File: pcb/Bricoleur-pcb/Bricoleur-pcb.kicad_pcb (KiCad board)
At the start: 2 copper layers, 78 parts, among them J1 USB_B_Micro, J2 Conn_02x10_Odd_Even, J3 Conn_02x03_Odd_Even, J4 Conn_02x03_Odd_Even, SW2 SW_Push, SW3 SW_Push, SW4 SW_Push, SW5 SW_Push, U1 Ultrasonic-LV-EZ0, U11 SW_DP3T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

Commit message: USB and some other connections, will probably require polish
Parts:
- moved L1 34.1 mm to (82.1, 119.6)
- moved U9 33.2 mm to (88.6, 117.3)
- moved J1 20.5 mm to (96.4, 115.6)
- moved R5 19.1 mm to (57.1, 170.3)
- moved R6 19.1 mm to (73.4, 170.3)
- moved R7 19.1 mm to (89.9, 170.3)
- moved SW4 19.1 mm to (60.4, 168.8)
- moved SW5 19.1 mm to (76.9, 168.8)
- moved SW2 19.1 mm to (38.9, 173.4)
- moved C14 19.1 mm to (56.9, 166.8)
- moved C16 19.1 mm to (90.4, 166.7)
- moved R1 19.1 mm to (41.6, 172.9)
- moved R11 19.1 mm to (57.1, 172.6)
- moved R12 19.1 mm to (73.4, 172.6)
- moved R13 19.1 mm to (89.9, 172.6)
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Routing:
- net VMCU: track 180.1 -> 294.1 mm, vias 12 -> 13
- net DH_#RESET: track 22.9 -> 91.4 mm, vias 0 -> 2
- net DEBUG_EXT_CABLE_ATTACH: track 0.00 -> 62.8 mm, vias 0 -> 2
- net DH_TCK_SWCLK: track 19.9 -> 77.0 mm, vias 0 -> 3
- net GND: track 210.4 -> 260.0 mm, vias 12 -> 11
- net Net-(C1-Pad2): track 10.2 -> 59.1 mm, vias 0 -> 2
- net /USB_D-: track 0.00 -> 42.3 mm, vias 0 -> 2
- net /USB_D+: track 0.00 -> 40.2 mm
- net DH_TDO_SWO: track 9.26 -> 48.6 mm, vias 0 -> 2
- net DH_TMS_SWDIO: track 9.20 -> 41.8 mm, vias 0 -> 2
- net DBG_PB_3: track 21.7 -> 53.5 mm
- net /sheet5BB7B6EA/INP: track 9.47 -> 38.7 mm
- net Net-(C2-Pad2): track 8.44 -> 37.3 mm, vias 0 -> 2
- net /Sheet5BB71F0E/INP: track 9.34 -> 37.7 mm
- net DBG_PB_1: track 21.1 -> 48.7 mm
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
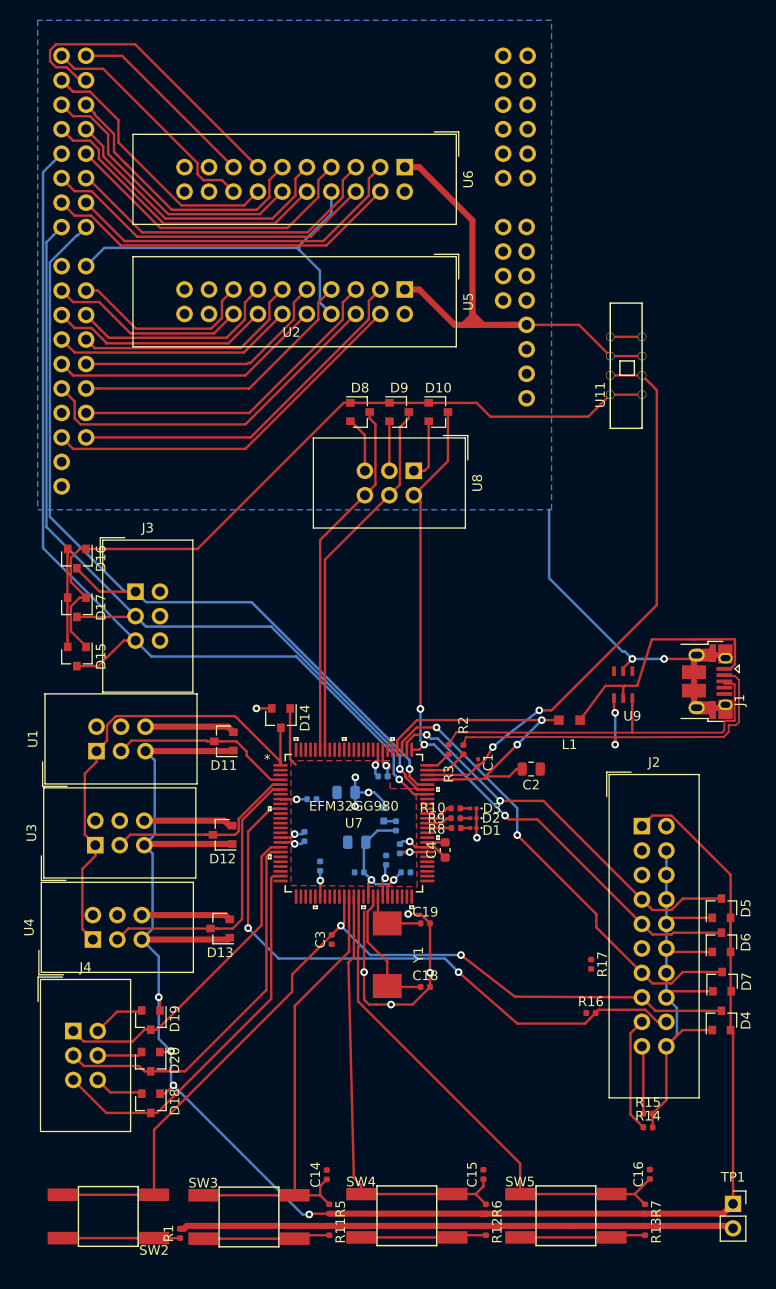
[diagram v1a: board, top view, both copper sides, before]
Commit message: Some routing tweaks
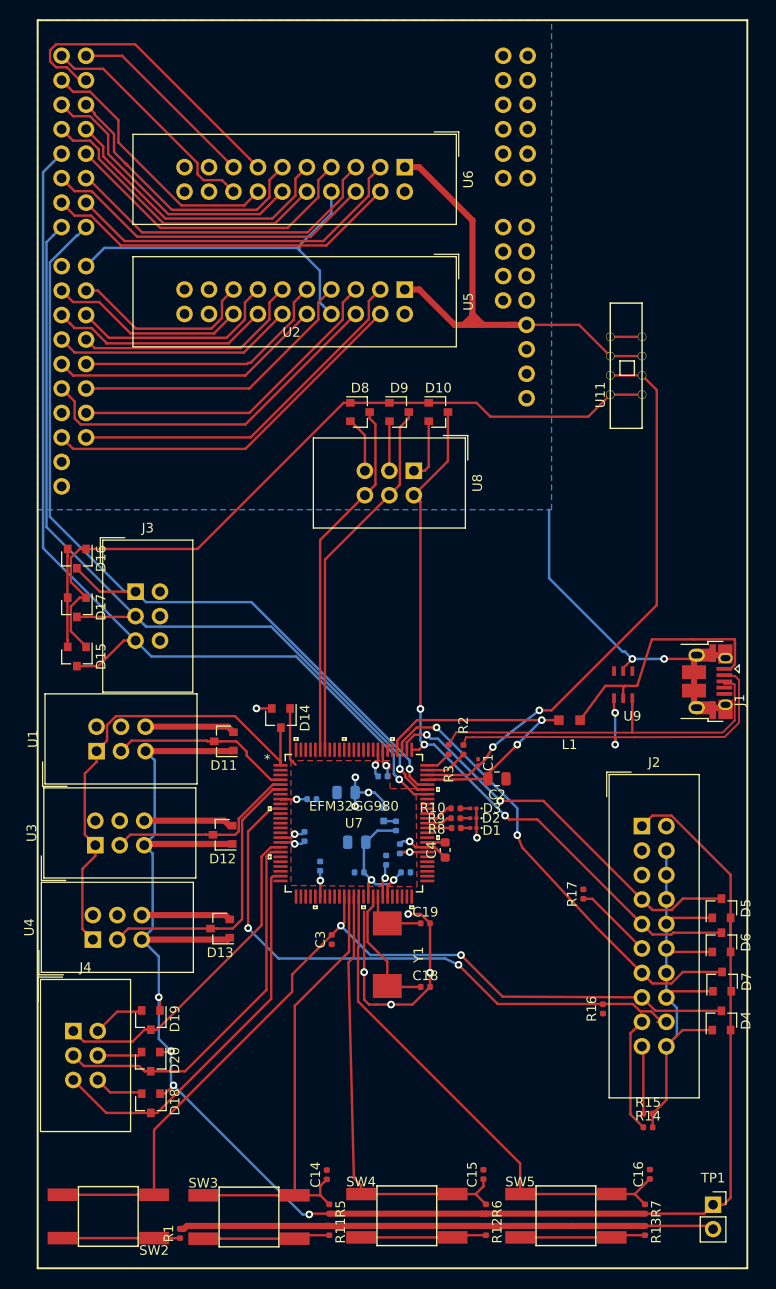
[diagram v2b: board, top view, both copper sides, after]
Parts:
- moved R17 7.33 mm to (83.5, 137.7), turned to 90 degrees
- moved C2 3.70 mm to (74.5, 125.7)
- moved TP1 2.08 mm to (97.0, 169.9)
- moved R16 1.32 mm to (85.5, 149.6), turned to 90 degrees
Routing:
- net Net-(J2-Pad11): track 0.00 -> 8.21 mm
- net Net-(C2-Pad2): track 37.3 -> 33.2 mm
- net GND: track 260.0 -> 258.0 mm
- net /USB_D+: track 40.2 -> 39.5 mm
- net /USB_D-: track 42.3 -> 41.7 mm

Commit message: Overwrite
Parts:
- moved TP1 73.7 mm to (72.6, 100.3), turned to 90 degrees
- moved SW2 35.2 mm to (57.8, 143.6), turned to 270 degrees
- moved R1 27.3 mm to (60.4, 153.1), turned to 0 degrees
- moved U11 23.9 mm to (72.6, 105.4), turned to 0 degrees
- moved D10 18.0 mm to (65.4, 105.4)
- moved D8 18.0 mm to (57.3, 105.4)
- moved D9 18.0 mm to (61.3, 105.4)
- moved U8 18.0 mm to (62.9, 111.5)
- moved J1 14.2 mm to (82.4, 117.9), turned to 90 degrees
- moved R16 10.7 mm to (74.9, 148.7), turned to 0 degrees
- moved U9 10.5 mm to (78.3, 119.6)
- moved C14 9.81 mm to (47.7, 163.2)
- moved C16 9.81 mm to (81.3, 163.2)
- moved R12 9.81 mm to (64.2, 169.0)
- moved R13 9.81 mm to (80.8, 169.0)
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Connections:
- net Net-(J1-Pad1) renamed /USB_5v
- net Net-(R2-Pad1) renamed /USB_R_D+
- net Net-(R3-Pad2) renamed /USB_R_D-
- R16 pad 1: PYNQ_3V3 -> VMCU
- U2 pad 50: /CAM0_DOUT2 -> /CAM0_DOUT3
- U2 pad 57: /CAM0_DOUT5 -> /CAM0_DOUT2
- U2 pad 58: /CAM0_DOUT3 -> /CAM0_DOUT5
- U9 pad 3: (no net) -> /USB_D+
- U9 pad 4: /USB_D+ -> (no net)
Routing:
- net VMCU: track 293.7 -> 342.9 mm, vias 13 -> 15
- net Net-(C1-Pad2): track 59.1 -> 26.2 mm, vias 2 -> 0
- net DH_#RESET: track 91.8 -> 60.0 mm, vias 2 -> 1
- net /USB_D-: track 41.7 -> 12.7 mm, vias 2 -> 0
- net GND: track 258.0 -> 286.8 mm, vias 11 -> 19
- net DH_TDO_SWO: track 48.3 -> 74.6 mm
- net /USB_D+: track 39.5 -> 14.0 mm
- net PYNQ_3V3: track 51.5 -> 72.8 mm
- net /USB_5v: track 26.8 -> 6.15 mm
- net DH_TMS_SWDIO: track 41.8 -> 61.6 mm
- net /sheet5BB7B6EA/INP: track 38.7 -> 19.6 mm
- net /Sheet5BB71F0E/INP: track 37.7 -> 18.6 mm
- net Net-(C2-Pad2): track 33.2 -> 16.6 mm, vias 2 -> 0
- net /CAM0_DOUT5: track 32.8 -> 22.6 mm
- net DEBUG_EXT_CABLE_ATTACH: track 62.6 -> 70.0 mm, vias 2 -> 1
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- added copper zone on F.Cu, net GND
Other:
- board outline added: 68.6 x 124.5 mm
- net class Power: trace_width 0.254 -> 0.635
- board text added: "OFF"
- board text added: "PYNQ"
- board text added: "USB"

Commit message: Layout finished.
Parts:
- moved SW3 113.6 mm to (148.3, 158.3), turned to 90 degrees
- moved R11 106.7 mm to (152.0, 145.2), turned to 0 degrees
- moved J4 104.8 mm to (134.8, 162.6), turned to 90 degrees
- moved R5 104.0 mm to (149.7, 145.2), turned to 0 degrees
- moved D18 103.8 mm to (142.3, 154.6), turned to 0 degrees
- moved C14 100.0 mm to (146.2, 145.5), turned to 180 degrees
- moved SW4 99.7 mm to (148.2, 141.9), turned to 90 degrees
- moved D20 99.4 mm to (138.0, 154.6), turned to 0 degrees
- moved R12 96.5 mm to (152.0, 129.0), turned to 0 degrees
- moved D19 95.2 mm to (133.7, 154.6), turned to 0 degrees
- moved U4 94.5 mm to (125.3, 160.6), turned to 180 degrees
- moved R6 93.5 mm to (149.7, 129.0), turned to 0 degrees
- moved R13 91.0 mm to (152.0, 112.5), turned to 0 degrees
- moved SW5 89.7 mm to (148.2, 125.4), turned to 90 degrees
- moved C15 88.9 mm to (146.2, 129.2), turned to 180 degrees
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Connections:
- U2 pad 29: /CAM1_HREF -> /CAM1_VSYNC
- U2 pad 36: /CAM1_VSYNC -> /CAM1_HREF
- U2 pad 44: /CAM0_SDATA -> /CAM0_DOUT2
- U2 pad 45: /CAM0_HREF -> /CAM0_DOUT5
- U2 pad 47: /CAM0_DOUT8 -> /CAM0_DOUT7
- U2 pad 48: /CAM0_DOUT6 -> /CAM0_DOUT9
- U2 pad 49: /CAM0_DOUT4 -> /CAM0_VSYNC
- U2 pad 50: /CAM0_DOUT3 -> /CAM0_SCL
- U2 pad 52: /CAM0_SCL -> /CAM0_DOUT4
- U2 pad 53: /CAM0_VSYNC -> /CAM0_DOUT3
- U2 pad 54: /CAM0_PCLK -> /CAM0_DOUT6
- U2 pad 55: /CAM0_DOUT9 -> /CAM0_DOUT8
- U2 pad 56: /CAM0_DOUT7 -> /CAM0_PCLK
- U2 pad 57: /CAM0_DOUT2 -> /CAM0_HREF
- U2 pad 58: /CAM0_DOUT5 -> /CAM0_SDATA
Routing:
- net GND: track 286.8 -> 241.7 mm, vias 19 -> 22
- net DH_TDO_SWO: track 74.6 -> 54.3 mm
- net DH_TCK_SWCLK: track 83.7 -> 65.3 mm
- net DEBUG_EXT_CABLE_ATTACH: track 70.0 -> 53.3 mm, vias 1 -> 2
- net VMCU: track 342.9 -> 326.7 mm, vias 15 -> 20
- net DH_TMS_SWDIO: track 61.6 -> 48.0 mm
- net DH_#RESET: track 60.0 -> 50.7 mm, vias 1 -> 2
- net /CAM0_DOUT4: track 27.7 -> 19.0 mm
- net /CAM0_DOUT6: track 29.8 -> 23.8 mm
- net /CAM0_DOUT3: track 22.6 -> 16.9 mm
- net /USB_D-: track 12.7 -> 18.0 mm
- net /CAM0_DOUT7: track 29.4 -> 24.6 mm
- net /CAM0_DOUT8: track 31.5 -> 26.9 mm
- net /CAM1_HREF: track 37.9 -> 33.4 mm
- net /CAM0_PCLK: track 32.3 -> 28.1 mm
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- removed copper zone on F.Cu, net GND
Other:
- board size 68.6 x 124.5 mm -> 124.5 x 66 mm
- net class USB added: clearance 0, trace_width 0.254, via_dia 0.8, via_drill 0.4

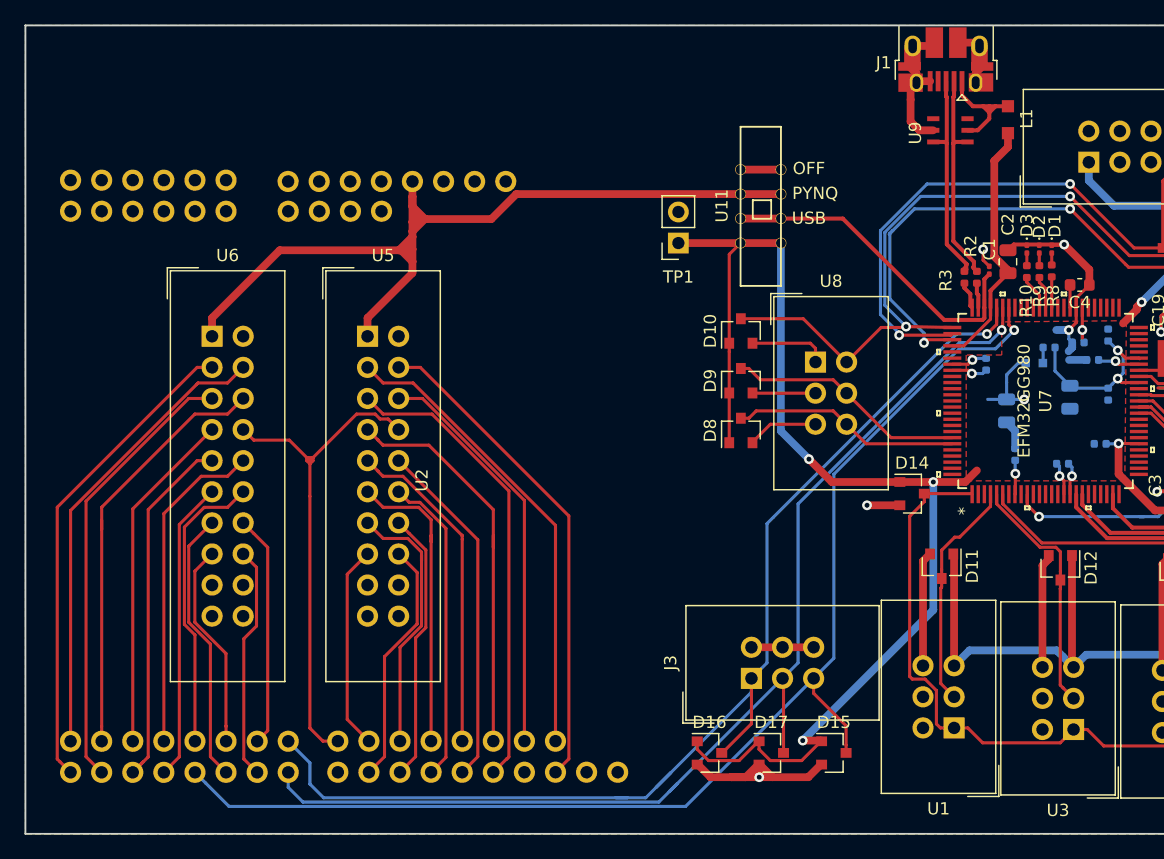
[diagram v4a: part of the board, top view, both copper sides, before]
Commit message: Header rotated - ethernet connector is too big.
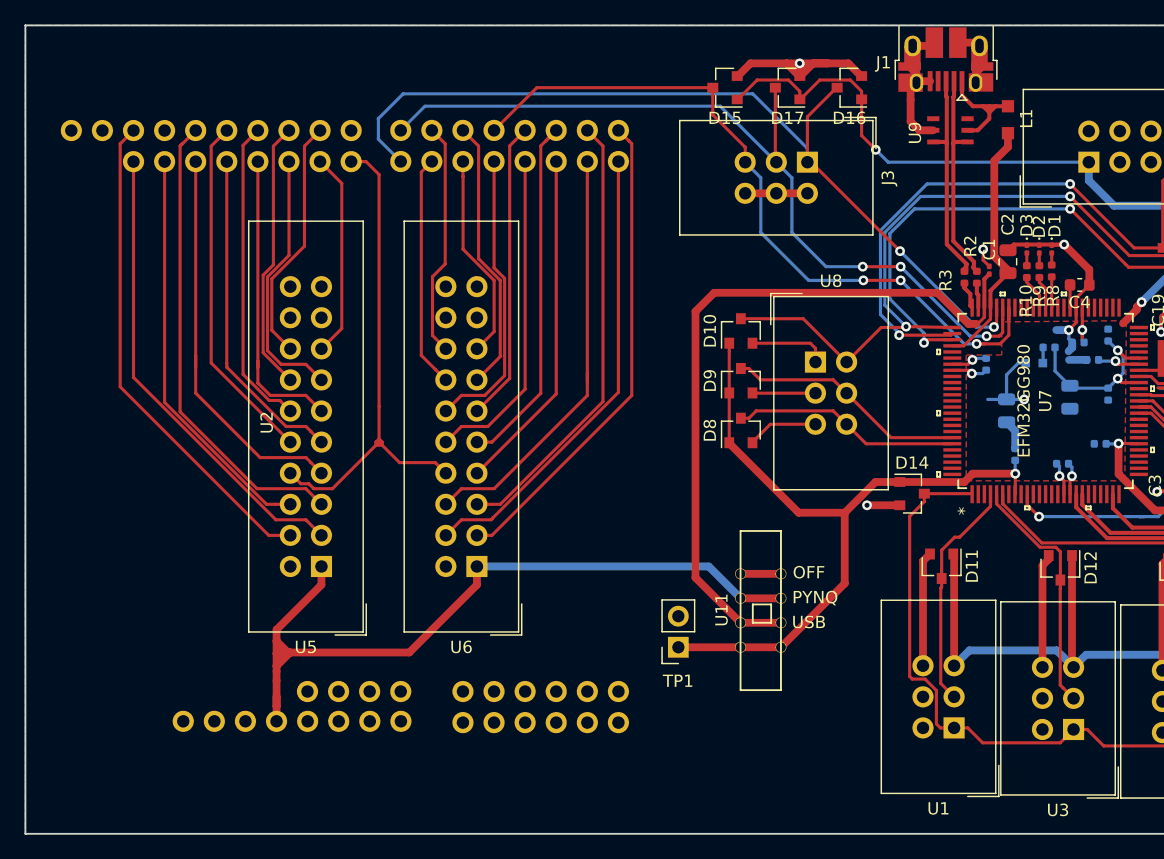
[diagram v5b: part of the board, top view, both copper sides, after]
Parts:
- moved D16 55.5 mm to (97.2, 107.9), turned to 180 degrees
- moved D15 55.1 mm to (87.1, 107.9), turned to 180 degrees
- moved D17 54.4 mm to (92.2, 107.9), turned to 180 degrees
- moved J3 42.4 mm to (93.8, 114.0), turned to 270 degrees
- moved TP1 33.0 mm to (83.3, 153.6)
- moved U11 33.0 mm to (88.3, 153.6)
- moved U6 28.7 mm to (66.8, 147.0), turned to 180 degrees
- moved U5 19.2 mm to (54.1, 147.0), turned to 180 degrees
- moved U2 12.9 mm to (50.4, 134.4), turned to 270 degrees
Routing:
- net /US0_CLK: track 102.9 -> 61.0 mm, vias 1 -> 3
- net Net-(C1-Pad2): track 27.2 -> 59.5 mm
- net /US0_RX: track 92.4 -> 68.7 mm, vias 1 -> 3
- net /US0_TX: track 96.4 -> 72.7 mm, vias 1 -> 2
- net VMCU: track 326.7 -> 314.2 mm, vias 20 -> 18
- net PYNQ_3V3: track 72.8 -> 64.0 mm
